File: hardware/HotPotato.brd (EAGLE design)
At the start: 38 x 27.3 mm, 14 parts, among them M1 SANYO_NRS-2574SMT, SW1 TACTILE-SWITCH-PTH, U1 TINY85-20-DIP

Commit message: Change LED package to 5mm
Fixes #2
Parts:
- D3: device SparkFun-LED:LED-1206 -> SparkFun-LED:LED5MM-KIT
- moved R2 23.5 mm to (100.4, 60.8)
- moved D3 0.70 mm to (96.1, 64.9), turned to 180 degrees
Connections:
- net GND: now also D3.K; no longer D3.C
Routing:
- net BUZZ: track 20.7 -> 45.8 mm
- net GND: track 19.4 -> 7.27 mm
- net N$2: track 15.9 -> 6.14 mm
- net VCC: track 68.3 -> 65.9 mm
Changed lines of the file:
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@@
 <elements>
 <element name="BATTERY_1" library="Itead_BP_110825.lbr" package="BATTERY_1236_C" value="BATTERY_1236_C" x="87.01" y="43.37"/>
-<element name="D3" library="SparkFun-LED" package="LED-1206" value="" x="96.17" y="65.595" smashed="yes">
-<attribute name="NAME" x="95.281" y="63.492" size="0.8128" layer="25"/>
-<attribute name="VALUE" x="95.154" y="63.817" size="0.4064" layer="27"/>
+<element name="D3" library="SparkFun-LED" package="LED5MM-KIT" value="" x="96.08" y="64.905" smashed="yes" rot="R180">
+<attribute name="NAME" x="93.219" y="66.508" size="0.8128" layer="25" rot="R180"/>
+<attribute name="VALUE" x="97.096" y="66.683" size="0.4064" layer="27" rot="R180"/>
 </element>
 <element name="M1" library="dhgoldberg" package="SMT" value="SANYO_NRS-2574SMT" x="100.58" y="54.57" smashed="yes" rot="R270"/>
@@
 <attribute name="VALUE" x="95.963" y="40.711" size="0.8128" layer="21"/>
 </element>
-<element name="R2" library="SparkFun-Passives" package="1206" value="220Ω" x="77.405" y="65.595" smashed="yes">
-<attribute name="NAME" x="75.135" y="63.738" size="0.8128" layer="25"/>
-<attribute name="VALUE" x="77.258" y="63.821" size="0.8128" layer="21"/>
+<element name="R2" library="SparkFun-Passives" package="1206" value="220Ω" x="100.405" y="60.845" smashed="yes">
+<attribute name="NAME" x="98.135" y="58.988" size="0.8128" layer="25"/>
+<attribute name="VALUE" x="100.258" y="59.071" size="0.8128" layer="21"/>
 </element>
 <element name="R3" library="SparkFun-Passives" package="1206" value="10K" x="81.045" y="43.87" smashed="yes" rot="R180">
@@
 <contactref element="D3" pad="A"/>
 <contactref element="R2" pad="2"/>
-<wire x1="78.805" y1="65.595" x2="94.67" y2="65.595" width="0.6096" layer="1"/>
+<wire x1="101.805" y1="60.845" x2="97.745" y2="64.905" width="0.6096" layer="1"/>
+<wire x1="97.745" y1="64.905" x2="97.35" y2="64.905" width="0.6096" layer="1"/>
 </signal>
 <signal name="SW">
@@
 <contactref element="BATTERY_1" pad="-"/>
 <contactref element="R4" pad="1"/>
-<contactref element="D3" pad="C"/>
+<contactref element="D3" pad="K"/>
 <contactref element="Q2" pad="3"/>
 <polygon width="0.4064" layer="16">
@@
 <vertex x="65.5" y="40"/>
 </polygon>
-<wire x1="87.01" y1="63.69" x2="87.2" y2="63.5" width="0.6096" layer="1"/>
-<wire x1="96.5" y1="63.5" x2="97.67" y2="64.67" width="0.6096" layer="1"/>
-<wire x1="97.67" y1="64.67" x2="97.67" y2="65.595" width="0.6096" layer="1"/>
-<wire x1="87.2" y1="63.5" x2="96.5" y2="63.5" width="0.6096" layer="1"/>
 <wire x1="67.061975" y1="50.073025" x2="67.595" y2="50.04" width="0.6096" layer="1"/>
 <wire x1="67.595" y1="50.04" x2="67.061975" y2="50.573025" width="0.6096" layer="1"/>
@@
 <contactref element="R5" pad="2"/>
 <contactref element="U1" pad="8"/>
-<wire x1="92.8" y1="61.5" x2="102" y2="61.5" width="0.6096" layer="1"/>
-<wire x1="92.8" y1="61.5" x2="84.5" y2="61.5" width="0.6096" layer="1"/>
 <wire x1="74.681975" y1="60.251978125" x2="73.78" y2="61.153953125" width="0.6096" layer="1"/>
 <wire x1="73.78" y1="62.755" x2="73.78" y2="61.153953125" width="0.6096" layer="1"/>
@@
 <wire x1="74.3" y1="63.3" x2="73.78" y2="62.78" width="0.6096" layer="1"/>
 <wire x1="73.78" y1="62.78" x2="73.78" y2="62.755" width="0.6096" layer="1"/>
-<wire x1="84.5" y1="61.5" x2="82.7" y2="63.3" width="0.6096" layer="1"/>
-<wire x1="102" y1="61.5" x2="102.9492" y2="60.5508" width="0.6096" layer="1"/>
-<wire x1="102.9492" y1="60.5508" x2="102.9492" y2="49" width="0.6096" layer="1"/>
-<wire x1="102.9492" y1="49" x2="101.8192" y2="47.87" width="0.6096" layer="1"/>
+<wire x1="82.7" y1="63.3" x2="84.5" y2="61.5" width="0.6096" layer="1"/>
+<wire x1="101.8192" y1="47.87" x2="102.9492" y2="49" width="0.6096" layer="1"/>
 <wire x1="101.8192" y1="47.87" x2="101.53" y2="47.87" width="0.6096" layer="1"/>
-<wire x1="92.6" y1="61.3" x2="92.6" y2="54.4" width="0.6096" layer="1"/>
-<wire x1="92.6" y1="61.3" x2="92.8" y2="61.5" width="0.6096" layer="1"/>
 <wire x1="87.01" y1="43.37" x2="87.9562" y2="44.3162" width="0.6096" layer="1"/>
 <wire x1="87.9562" y1="51.2394" x2="87.9562" y2="44.3162" width="0.6096" layer="1"/>
 <wire x1="92.6" y1="54.4" x2="89.4394" y2="51.2394" width="0.6096" layer="1"/>
 <wire x1="89.4394" y1="51.2394" x2="87.9562" y2="51.2394" width="0.6096" layer="1"/>
+<wire x1="84.5" y1="61.5" x2="92.6" y2="61.5" width="0.6096" layer="1"/>
+<wire x1="92.6" y1="59" x2="92.6" y2="61.5" width="0.6096" layer="1"/>
+<wire x1="92.6" y1="59" x2="92.6" y2="54.4" width="0.6096" layer="1"/>
+<wire x1="102.9492" y1="58.5" x2="102.4492" y2="59" width="0.6096" layer="1"/>
+<wire x1="102.4492" y1="59" x2="92.6" y2="59" width="0.6096" layer="1"/>
+<wire x1="102.9492" y1="49" x2="102.9492" y2="58.5" width="0.6096" layer="1"/>
 </signal>
 <signal name="N$5">
@@
 <contactref element="R2" pad="1"/>
 <wire x1="72.4" y1="54.913953125" x2="72.4" y2="64.4" width="0.6096" layer="1"/>
-<wire x1="72.4" y1="64.4" x2="73.595" y2="65.595" width="0.6096" layer="1"/>
-<wire x1="73.595" y1="65.595" x2="76.005" y2="65.595" width="0.6096" layer="1"/>
 <wire x1="74.681975" y1="52.631978125" x2="72.4" y2="54.913953125" width="0.6096" layer="1"/>
 <wire x1="74.31" y1="48.91" x2="74.681975" y2="49.281975" width="0.6096" layer="1"/>
 <wire x1="74.681975" y1="49.281975" x2="74.681975" y2="52.631978125" width="0.6096" layer="1"/>
+<wire x1="73.75" y1="65.75" x2="91" y2="65.75" width="0.6096" layer="1"/>
+<wire x1="91" y1="65.75" x2="95.905" y2="60.845" width="0.6096" layer="1"/>
+<wire x1="95.905" y1="60.845" x2="99.005" y2="60.845" width="0.6096" layer="1"/>
+<wire x1="72.4" y1="64.4" x2="73.75" y2="65.75" width="0.6096" layer="1"/>
 </signal>
 <signal name="MOT">

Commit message: Add reset button
Fixes #1
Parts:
- added K1: TS-1101F, Seeed-OPL-Button:SW2-3.4X6.0X3.55MM-90D
- moved R4 0.71 mm to (67.1, 48.1)
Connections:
- removed net RST: R5.1, U1.1
- new net N$6: K1.P$1, R5.1, U1.1
- net GND: now also K1.P$2
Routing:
- net N$6: track 0.00 -> 9.75 mm
- net RST: track 4.95 -> 0.00 mm
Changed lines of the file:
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@@
 <layer number="132" name="bAdjust" color="7" fill="1" visible="yes" active="yes"/>
 <layer number="133" name="bottom_silk" color="7" fill="1" visible="yes" active="yes"/>
+<layer number="134" name="silk_top" color="7" fill="1" visible="no" active="no"/>
+<layer number="135" name="silk_bottom" color="7" fill="1" visible="no" active="no"/>
+<layer number="136" name="silktop" color="7" fill="1" visible="yes" active="yes"/>
+<layer number="137" name="silkbottom" color="7" fill="1" visible="yes" active="yes"/>
 <layer number="144" name="Drill_legend" color="7" fill="1" visible="yes" active="yes"/>
+<layer number="145" name="DrillLegend_01-16" color="7" fill="1" visible="yes" active="yes"/>
+<layer number="146" name="DrillLegend_01-20" color="7" fill="1" visible="yes" active="yes"/>
 <layer number="150" name="Notes" color="7" fill="1" visible="yes" active="yes"/>
 <layer number="151" name="HeatSink" color="7" fill="1" visible="yes" active="yes"/>
@@
 </autorouter>
 <elements>
-<element name="BATTERY_1" library="Itead_BP_110825.lbr" package="BATTERY_1236_C" value="BATTERY_1236_C" x="87.01" y="43.37"/>
+<element name="BATTERY_1" library="Itead_BP_110825.lbr" package="BATTERY_1236_C" value="BATTERY_1236_C" x="87.01" y="43.37" smashed="yes">
+<attribute name="NAME" x="82.33" y="60" size="0.8128" layer="25" ratio="10"/>
+<attribute name="VALUE" x="82.32" y="58.25" size="0.8128" layer="27" ratio="10"/>
+</element>
 <element name="D3" library="SparkFun-LED" package="LED5MM-KIT" value="" x="96.08" y="64.905" smashed="yes" rot="R180">
 <attribute name="NAME" x="93.219" y="66.508" size="0.8128" layer="25" rot="R180"/>
@@
 <attribute name="VALUE" x="82.442" y="45.644" size="0.8128" layer="21" rot="R180"/>
 </element>
-<element name="R4" library="SparkFun-Passives" package="1206" value="22Ω" x="67.595" y="48.64" smashed="yes" rot="R270">
-<attribute name="NAME" x="68.738" y="47.66" size="0.8128" layer="25" rot="R270"/>
-<attribute name="VALUE" x="68.571" y="50.787" size="0.8128" layer="21" rot="R270"/>
+<element name="R4" library="SparkFun-Passives" package="1206" value="22Ω" x="67.095" y="48.14" smashed="yes" rot="R270">
+<attribute name="NAME" x="68.238" y="47.16" size="0.8128" layer="25" rot="R270"/>
+<attribute name="VALUE" x="68.071" y="50.287" size="0.8128" layer="21" rot="R270"/>
 </element>
 <element name="R5" library="SparkFun-Passives" package="1206" value="10K" x="72.38" y="62.755" smashed="yes">
-<attribute name="NAME" x="70.11" y="63.898" size="0.8128" layer="25"/>
-<attribute name="VALUE" x="72.733" y="63.981" size="0.8128" layer="21"/>
+<attribute name="NAME" x="69.86" y="63.898" size="0.8128" layer="25"/>
+<attribute name="VALUE" x="74.983" y="62.481" size="0.8128" layer="21"/>
 </element>
 <element name="SW1" library="GeekAmmo" package="TAC-SWITCH-PTH" value="TACTILE-SWITCH-PTH" x="84.705" y="53.5" smashed="yes" rot="MR0">
@@
 </element>
 <element name="U1" library="SparkFun-DigitalIC" package="DIP08" value="TINY85-20-DIP" x="70.871975" y="56.441978125" smashed="yes" rot="R270">
-<attribute name="NAME" x="67.061975" y="62.156978125" size="1.27" layer="25" ratio="10"/>
+<attribute name="NAME" x="66.311975" y="61.656978125" size="1.27" layer="25" ratio="10"/>
 <attribute name="PROD_ID" value="IC-09445" x="70.871975" y="56.441978125" size="1.778" layer="27" rot="R270" display="off"/>
 <attribute name="VALUE" x="68.736975" y="59.366978125" size="0.4064" layer="27" ratio="10" rot="R270"/>
@@
 </element>
 <element name="U$1" library="adafruit" package="OSHWLOGO_BACK_0.2" value="" x="95.8" y="57.1"/>
+<element name="K1" library="Seeed-OPL-Button" package="SW2-3.4X6.0X3.55MM-90D" value="TS-1101F" x="75.5" y="65.75" smashed="yes" rot="R180">
+<attribute name="MPN" value="TS-1101F" x="75.5" y="65.75" size="1.778" layer="27" rot="R180" display="off"/>
+<attribute name="NAME" x="81.155" y="66.345" size="0.889" layer="25" ratio="11" rot="R180"/>
+<attribute name="VALUE" x="83.405" y="68.195" size="0.6096" layer="27" ratio="11" rot="R180"/>
+</element>
 </elements>
 <signals>
@@
 <vertex x="65.5" y="40"/>
 </polygon>
-<wire x1="67.061975" y1="50.073025" x2="67.595" y2="50.04" width="0.6096" layer="1"/>
-<wire x1="67.595" y1="50.04" x2="67.061975" y2="50.573025" width="0.6096" layer="1"/>
-<wire x1="67.061975" y1="50.573025" x2="67.061975" y2="52.631978125" width="0.6096" layer="1"/>
 <contactref element="J1" pad="5"/>
 <wire x1="79.645" y1="43.87" x2="79.75" y2="43.975" width="0.6096" layer="1"/>
 <wire x1="82.31" y1="41.2" x2="82.31" y2="41.205" width="0.6096" layer="1"/>
 <wire x1="82.31" y1="41.205" x2="79.645" y2="43.87" width="0.6096" layer="1"/>
+<contactref element="K1" pad="P$2"/>
+<wire x1="67.095" y1="49.54" x2="67.061975" y2="49.573025" width="0.6096" layer="1"/>
+<wire x1="67.061975" y1="49.573025" x2="67.061975" y2="52.631978125" width="0.6096" layer="1"/>
 </signal>
 <signal name="VCC">
@@
 <contactref element="R4" pad="2"/>
 <contactref element="SG2" pad="P$2"/>
-<wire x1="68.26" y1="47.24" x2="67.595" y2="47.24" width="0.6096" layer="1"/>
-<wire x1="67.595" y1="47.24" x2="69.925" y2="44.91" width="0.6096" layer="1"/>
-<wire x1="69.925" y1="44.91" x2="74.31" y2="44.91" width="0.6096" layer="1"/>
+<wire x1="67.095" y1="46.74" x2="68.925" y2="44.91" width="0.6096" layer="1"/>
+<wire x1="68.925" y1="44.91" x2="74.31" y2="44.91" width="0.6096" layer="1"/>
 </signal>
 <signal name="BUZZ">
@@
 <contactref element="U1" pad="5"/>
 <contactref element="R2" pad="1"/>
-<wire x1="72.4" y1="54.913953125" x2="72.4" y2="64.4" width="0.6096" layer="1"/>
 <wire x1="74.681975" y1="52.631978125" x2="72.4" y2="54.913953125" width="0.6096" layer="1"/>
 <wire x1="74.31" y1="48.91" x2="74.681975" y2="49.281975" width="0.6096" layer="1"/>
 <wire x1="74.681975" y1="49.281975" x2="74.681975" y2="52.631978125" width="0.6096" layer="1"/>
-<wire x1="73.75" y1="65.75" x2="91" y2="65.75" width="0.6096" layer="1"/>
-<wire x1="91" y1="65.75" x2="95.905" y2="60.845" width="0.6096" layer="1"/>
+<wire x1="95.905" y1="60.845" x2="91" y2="65.75" width="0.6096" layer="1"/>
 <wire x1="95.905" y1="60.845" x2="99.005" y2="60.845" width="0.6096" layer="1"/>
-<wire x1="72.4" y1="64.4" x2="73.75" y2="65.75" width="0.6096" layer="1"/>
+<wire x1="80.5" y1="65.75" x2="79" y2="64.25" width="0.6096" layer="1"/>
+<wire x1="72.75" y1="64.25" x2="79" y2="64.25" width="0.6096" layer="1"/>
+<wire x1="91" y1="65.75" x2="80.5" y2="65.75" width="0.6096" layer="1"/>
+<wire x1="72.4" y1="54.913953125" x2="72.4" y2="63.9" width="0.6096" layer="1"/>
+<wire x1="72.4" y1="63.9" x2="72.75" y2="64.25" width="0.6096" layer="1"/>
 </signal>
 <signal name="MOT">
@@
 <wire x1="76" y1="44.5" x2="74.75" y2="43.25" width="0.6096" layer="1"/>
 </signal>
-<signal name="RST">
-<contactref element="U1" pad="1"/>
-<contactref element="R5" pad="1"/>
-<wire x1="67.061975" y1="60.251978125" x2="69.564996875" y2="62.755" width="0.6096" layer="1"/>
-<wire x1="69.564996875" y1="62.755" x2="70.98" y2="62.755" width="0.6096" layer="1"/>
-</signal>
 <signal name="N$3">
 <contactref element="M1" pad="P$2"/>
@@
 <wire x1="77.25" y1="46.75" x2="77.25" y2="43.75" width="0.6096" layer="1"/>
 </signal>
+<signal name="N$6">
+<contactref element="U1" pad="1"/>
+<contactref element="R5" pad="1"/>
+<contactref element="K1" pad="P$1"/>
+<wire x1="67.061975" y1="60.251978125" x2="69.564996875" y2="62.755" width="0.6096" layer="1"/>
+<wire x1="69.564996875" y1="62.755" x2="70.98" y2="62.755" width="0.6096" layer="1"/>
+<wire x1="70.98" y1="62.755" x2="71" y2="62.775" width="0.6096" layer="1"/>
+<wire x1="71" y1="62.775" x2="71" y2="64.5" width="0.6096" layer="1"/>
+<wire x1="71" y1="64.5" x2="72.377" y2="65.877" width="0.6096" layer="1"/>
+<wire x1="72.377" y1="65.877" x2="73.468" y2="65.877" width="0.6096" layer="1"/>
+</signal>
 </signals>

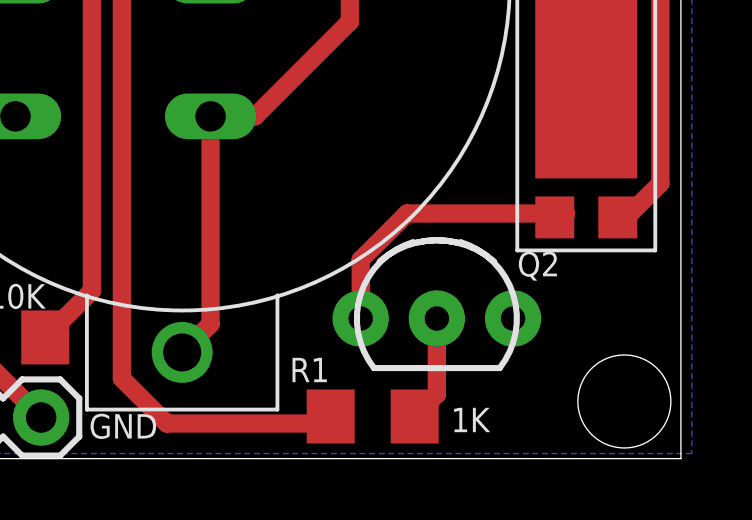
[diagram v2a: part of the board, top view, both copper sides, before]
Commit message: Change board name and board revision
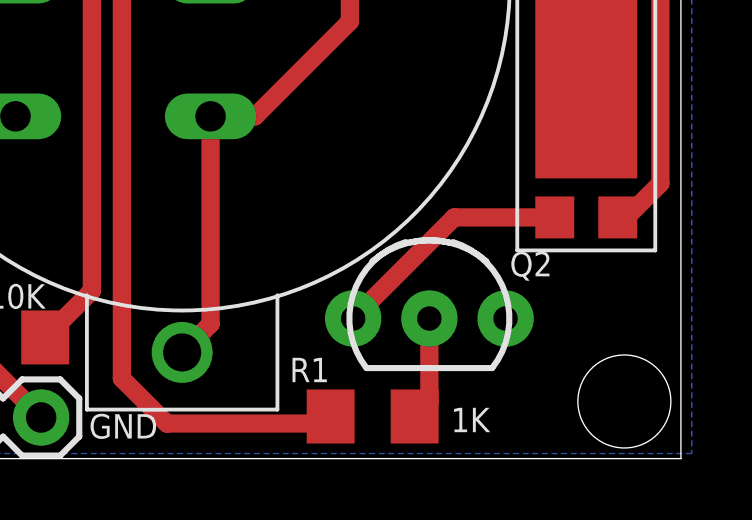
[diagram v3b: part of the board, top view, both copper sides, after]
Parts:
- moved Q2 0.25 mm to (95.2, 44.5)
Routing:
- net N$3: track 9.83 -> 8.12 mm
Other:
- board text added: "Scrumtato"
- board text added: "rev. 1 designed by Dimitris Platis"
- board text removed: "HotPotato"
- board text removed: "rev. 0 designed by Dimitris Platis"
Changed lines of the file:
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@@
 <text x="83.9" y="40.5" size="0.8128" layer="21" font="vector">GND</text>
 <text x="72.65" y="42.9" size="0.8128" layer="21" font="vector">ACC_X</text>
-<text x="102.7" y="52.8" size="1.9304" layer="22" font="vector" rot="MR0">HotPotato</text>
-<text x="95.8" y="48.3" size="1.016" layer="22" font="vector" rot="MR0" align="bottom-center">rev. 0
+<text x="102.7" y="52.8" size="1.9304" layer="22" font="vector" rot="MR0">Scrumtato</text>
+<text x="95.8" y="48.3" size="1.016" layer="22" font="vector" rot="MR0" align="bottom-center">rev. 1
 designed by
 Dimitris Platis</text>
@@
 </element>
 <element name="SG2" library="dhgoldberg" package="BUZZER-9MM-PTH" value="BUZZER" x="74.31" y="46.91" rot="R270"/>
-<element name="Q2" library="SparkFun-DiscreteSemi" package="TO-92-AMMO" value="" x="95.5" y="44.5" smashed="yes">
-<attribute name="NAME" x="98.175" y="45.905" size="0.8128" layer="25" ratio="10"/>
-<attribute name="VALUE" x="98.675" y="42.595" size="0.4064" layer="27" ratio="10"/>
+<element name="Q2" library="SparkFun-DiscreteSemi" package="TO-92-AMMO" value="" x="95.25" y="44.5" smashed="yes">
+<attribute name="NAME" x="97.925" y="45.905" size="0.8128" layer="25" ratio="10"/>
+<attribute name="VALUE" x="98.425" y="42.595" size="0.4064" layer="27" ratio="10"/>
 </element>
 <element name="J1" library="SparkFun-Connectors" package="1X05" value="" x="72.15" y="41.2" smashed="yes">
@@
 <contactref element="M1" pad="P$2"/>
 <contactref element="Q2" pad="1"/>
-<wire x1="99.8" y1="48" x2="94.5" y2="48" width="0.6096" layer="1"/>
-<wire x1="99.8" y1="48" x2="99.43" y2="47.87" width="0.6096" layer="1"/>
-<wire x1="92.96" y1="46.46" x2="92.96" y2="44.5" width="0.6096" layer="1"/>
-<wire x1="94.5" y1="48" x2="92.96" y2="46.46" width="0.6096" layer="1"/>
+<wire x1="92.71" y1="44.5" x2="96.08" y2="47.87" width="0.6096" layer="1"/>
+<wire x1="96.08" y1="47.87" x2="99.43" y2="47.87" width="0.6096" layer="1"/>
 </signal>
 <signal name="N$4">
 <contactref element="R1" pad="2"/>
 <contactref element="Q2" pad="2"/>
-<wire x1="94.76" y1="41.235" x2="95.5" y2="41.975" width="0.6096" layer="1"/>
-<wire x1="95.5" y1="41.975" x2="95.5" y2="44.5" width="0.6096" layer="1"/>
+<wire x1="94.76" y1="41.235" x2="95.25" y2="41.725" width="0.6096" layer="1"/>
+<wire x1="95.25" y1="41.725" x2="95.25" y2="44.5" width="0.6096" layer="1"/>
 </signal>
 <signal name="ACC_IN">

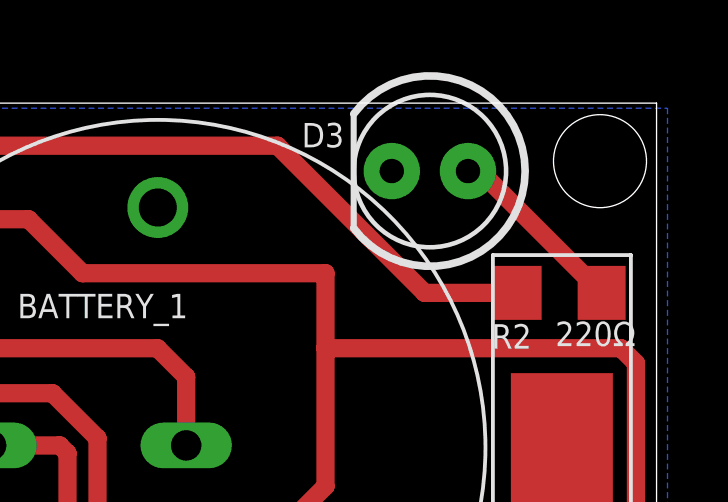
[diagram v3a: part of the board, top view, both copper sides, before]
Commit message: Small mainly commodity fixes
Changing orientation of D3, placement of R4, SW1 part number placement
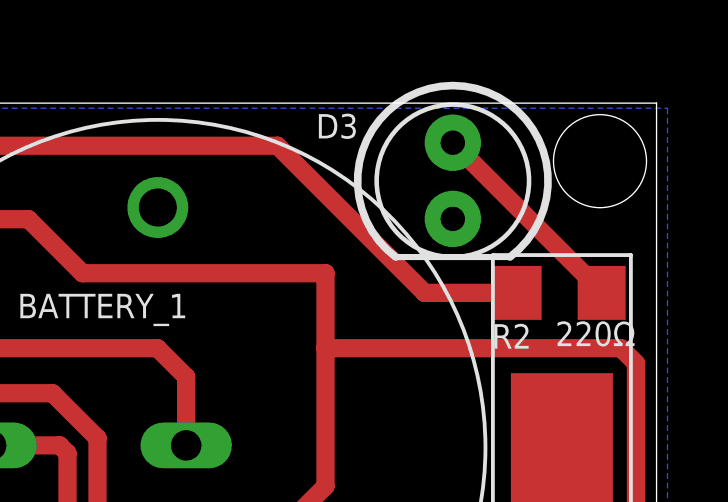
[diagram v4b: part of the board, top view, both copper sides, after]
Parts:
- moved D3 0.83 mm to (96.8, 64.6), turned to 270 degrees
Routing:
- net N$2: track 6.14 -> 7.06 mm
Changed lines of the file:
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@@
 <attribute name="VALUE" x="82.32" y="58.25" size="0.8128" layer="27" ratio="10"/>
 </element>
-<element name="D3" library="SparkFun-LED" package="LED5MM-KIT" value="" x="96.08" y="64.905" smashed="yes" rot="R180">
-<attribute name="NAME" x="93.219" y="66.508" size="0.8128" layer="25" rot="R180"/>
-<attribute name="VALUE" x="97.096" y="66.683" size="0.4064" layer="27" rot="R180"/>
+<element name="D3" library="SparkFun-LED" package="LED5MM-KIT" value="" x="96.845" y="64.58" smashed="yes" rot="R270">
+<attribute name="NAME" x="92.281" y="65.992" size="0.8128" layer="25"/>
+<attribute name="VALUE" x="95.067" y="65.596" size="0.4064" layer="27" rot="R270"/>
 </element>
 <element name="M1" library="dhgoldberg" package="SMT" value="SANYO_NRS-2574SMT" x="100.58" y="54.57" smashed="yes" rot="R270"/>
@@
 </element>
 <element name="SW1" library="GeekAmmo" package="TAC-SWITCH-PTH" value="TACTILE-SWITCH-PTH" x="84.705" y="53.5" smashed="yes" rot="MR0">
-<attribute name="NAME" x="81.045" y="52.91" size="1.27" layer="26" ratio="10" rot="MR0"/>
+<attribute name="NAME" x="85.795" y="53.16" size="0.8128" layer="26" ratio="10" rot="MR0"/>
 </element>
 <element name="U1" library="SparkFun-DigitalIC" package="DIP08" value="TINY85-20-DIP" x="70.871975" y="56.441978125" smashed="yes" rot="R270">
@@
 <contactref element="D3" pad="A"/>
 <contactref element="R2" pad="2"/>
-<wire x1="101.805" y1="60.845" x2="97.745" y2="64.905" width="0.6096" layer="1"/>
-<wire x1="97.745" y1="64.905" x2="97.35" y2="64.905" width="0.6096" layer="1"/>
+<wire x1="101.805" y1="60.845" x2="101.805" y2="60.89" width="0.6096" layer="1"/>
+<wire x1="101.805" y1="60.89" x2="96.845" y2="65.85" width="0.6096" layer="1"/>
 </signal>
 <signal name="SW">
